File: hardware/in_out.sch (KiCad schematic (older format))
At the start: 41 parts

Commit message: changed heirarchy labels, changed diode and inductor to standard library symbols
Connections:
- net pd0_i2c_scl renamed i2c_scl
- net pd1_i2c_sda renamed i2c_sda
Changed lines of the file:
@@
-EESchema Schematic File Version 2  date Thu 31 Oct 2013 01:30:22 PM EDT
+EESchema Schematic File Version 2  date Mon 04 Nov 2013 07:38:03 AM EST
 LIBS:power
 LIBS:device
@@
 Sheet 4 5
 Title ""
-Date "31 oct 2013"
+Date "4 nov 2013"
 Rev ""
 Comp ""
@@
 $EndComp
 Text HLabel 1450 5700 0    60   Input ~ 0
-pd1_i2c_sda
+i2c_sda
 Text HLabel 1450 5550 0    60   Input ~ 0
-pd0_i2c_scl
+i2c_scl
 $Comp
 L +3.3V #PWR?

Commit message: cleaned up most of the error check problems
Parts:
- gave numbers to parts that had none: 41
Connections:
- no-connect marks 0 -> 4

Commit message: added RCT and accellerometer, added new sheet
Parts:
- removed C15, C16: 3000 uF, symbol C
- removed D4, D5, D6, D7: BAT54J, 1206, symbol BAT54J
- removed R18, R22: 1K, symbol R
- removed R21, R23: 220, symbol R
- removed R24, R36: 10K, symbol R
- removed R25, R38: 33.2K, symbol R
- removed T1, T2: BUZ11, symbol BUZ11
- removed U7, U8: SN74LVC1G14, symbol SN74LVC1G14
- added BT?: BATTERY, symbol BATTERY
- added C? (x3): 0.1 uF, symbol C
- added C?: 4.7 uF, symbol C
- added R? (x3): 2K, symbol R
- added U?: DS1307, symbol DS1307
- added U?: MMA8451Q, symbol MMA8451Q
- added X?: 32.768KHz, symbol CRYSTAL
- R23: renamed from R19; value 1K -> 2K
- R24: renamed from R20; value 1K -> 2K
- renumbered C14 to C19, Q1 to Q4, Q2 to Q5, Q3 to Q6, Q4 to Q7, R16 to R20, R17 to R21, R26 to R30, R27 to R31, R28 to R32, R29 to R33, R30 to R34, R31 to R35, R32 to R36, R33 to R37, R34 to R38, R35 to R39, R37 to R41, R39 to R43
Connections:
- net +3.3V: now also R?.1, R?.1, U?.1 (Vddio), U?.14 (Vdd)
- net +5V: now also C?.1, C?.1, R?.1, U?.8 (Vcc)
- net GND: now also BT?.2 (-), C?.2, C?.2, C?.2, C?.2, U?.10 (gnd), U?.12 (gnd), U?.4 (gnd), U?.5 (gnd)
- net i2c_scl: now also U?.4 (scl), U?.6 (scl)
- net i2c_sda: now also U?.5 (sda), U?.6 (sda)
- new net: U?.1 (X1), X?.1
- new net: U?.2 (X2), X?.2
- new net: BT?.1 (+), U?.3 (Vbat)
- new net: C?.1, U?.2 (byp)
- new net accel_int_0: R?.2, U?.11 (int1)
- new net accel_int_1: R?.2, U?.9 (int2)
- new net square_wave: R?.2, U?.7 (sqw_out)
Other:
- note added: "12.5 pF\n"
- note added: "Li 48 >48 mA"
- moved on the sheet: C19, P2, Q4, Q5, Q6, Q7, R20, R21, R23, R24, R30, R31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

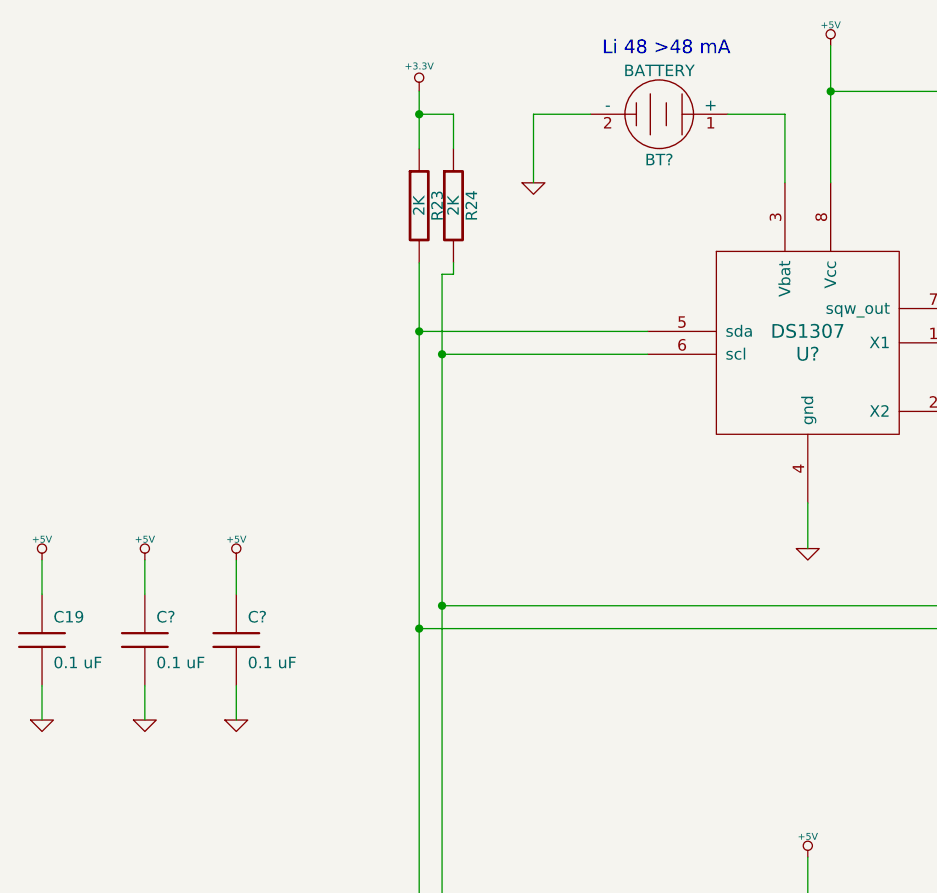
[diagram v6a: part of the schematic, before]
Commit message: fixed heirarchy connections for modified sheets
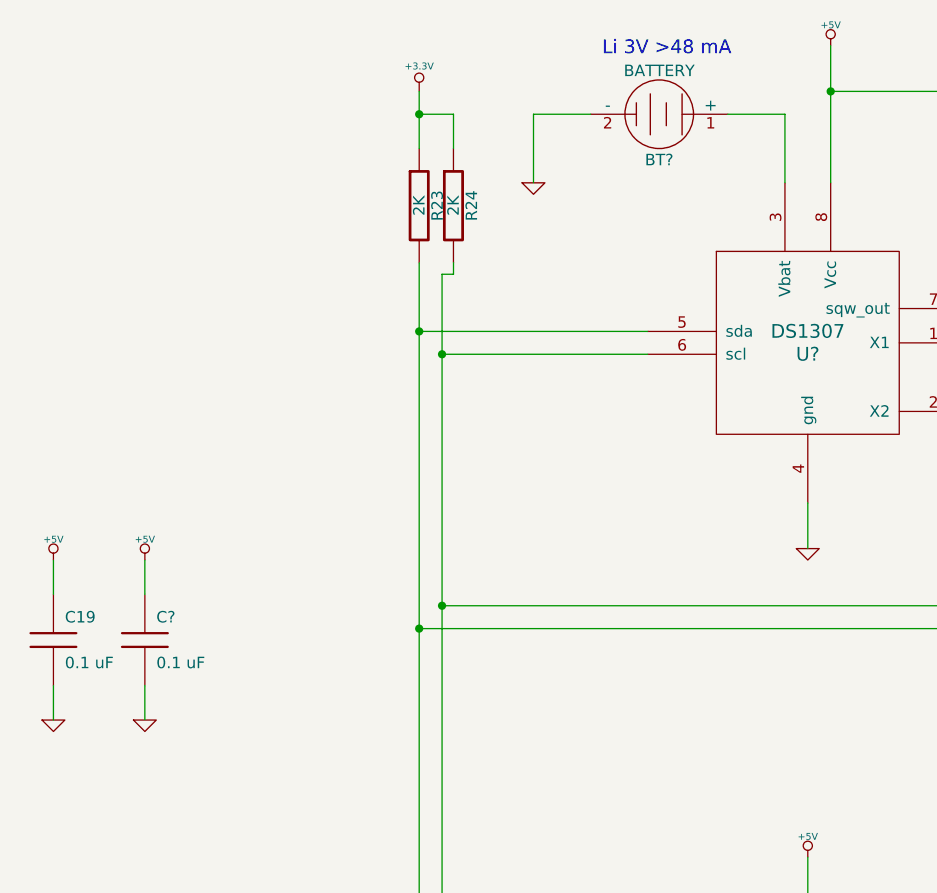
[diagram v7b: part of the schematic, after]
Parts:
- removed C?: 0.1 uF, symbol C
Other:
- note added: "Li 3V >48 mA"
- note removed: "Li 48 >48 mA"
- moved on the sheet: C19
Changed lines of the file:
@@
-EESchema Schematic File Version 2  date Tue 12 Nov 2013 10:09:33 PM EST
+EESchema Schematic File Version 2  date Wed 13 Nov 2013 08:13:39 AM EST
 LIBS:power
 LIBS:device
@@
 	6650 2200 7850 2200
 Wire Wire Line
-	1700 3600 1700 3750
-Wire Wire Line
-	1700 3200 1700 3050
-Wire Wire Line
 	1300 3200 1300 3050
 Wire Wire Line
@@
 	4300 1400 4300 800
 Wire Wire Line
-	850  3600 850  3750
+	900  3600 900  3750
 Wire Wire Line
 	1200 6250 1200 6500
@@
 	1350 6300 1350 6250
 Wire Wire Line
-	850  3200 850  3050
+	900  3200 900  3050
 Wire Wire Line
 	4200 3000 4200 2800
@@
 $EndComp
 $Comp
-L GND #PWR?
-U 1 1 5282D633
-P 1700 3750
-F 0 "#PWR?" H 1700 3750 30  0001 C CNN
-F 1 "GND" H 1700 3680 30  0001 C CNN
-	1    1700 3750
-	1    0    0    -1
-$EndComp
-$Comp
-L +5V #PWR?
-U 1 1 5282D632
-P 1700 3050
-F 0 "#PWR?" H 1700 3140 20  0001 C CNN
-F 1 "+5V" H 1700 3140 30  0000 C CNN
-	1    1700 3050
-	1    0    0    -1
-$EndComp
-$Comp
-L C C?
-U 1 1 5282D631
-P 1700 3400
-F 0 "C?" H 1750 3500 50  0000 L CNN
-F 1 "0.1 uF" H 1750 3300 50  0000 L CNN
-	1    1700 3400
-	1    0    0    -1
-$EndComp
-$Comp
 L C C?
 U 1 1 5282D617
@@
 $EndComp
 Text Notes 3300 850  0    60   ~ 0
-Li 48 >48 mA
+Li 3V >48 mA
 Text Notes 5800 2750 0    60   ~ 0
 12.5 pF\n
@@
 L GND #PWR022
 U 1 1 526E4C5E
-P 850 3750
-F 0 "#PWR022" H 850 3750 30  0001 C CNN
-F 1 "GND" H 850 3680 30  0001 C CNN
-	1    850  3750
+P 900 3750
+F 0 "#PWR022" H 900 3750 30  0001 C CNN
+F 1 "GND" H 900 3680 30  0001 C CNN
+	1    900  3750
 	1    0    0    -1
 $EndComp
@@
 L +5V #PWR023
 U 1 1 526E4C55
-P 850 3050
-F 0 "#PWR023" H 850 3140 20  0001 C CNN
-F 1 "+5V" H 850 3140 30  0000 C CNN
-	1    850  3050
+P 900 3050
+F 0 "#PWR023" H 900 3140 20  0001 C CNN
+F 1 "+5V" H 900 3140 30  0000 C CNN
+	1    900  3050
 	1    0    0    -1
 $EndComp
@@
 L C C19
 U 1 1 526E4C4C
-P 850 3400
-F 0 "C19" H 900 3500 50  0000 L CNN
-F 1 "0.1 uF" H 900 3300 50  0000 L CNN
-	1    850  3400
-	1    0    0    -1
-$EndComp
+P 900 3400
+F 0 "C19" H 950 3500 50  0000 L CNN
+F 1 "0.1 uF" H 950 3300 50  0000 L CNN
+	1    900  3400
+	1    0    0    -1
+$EndComp

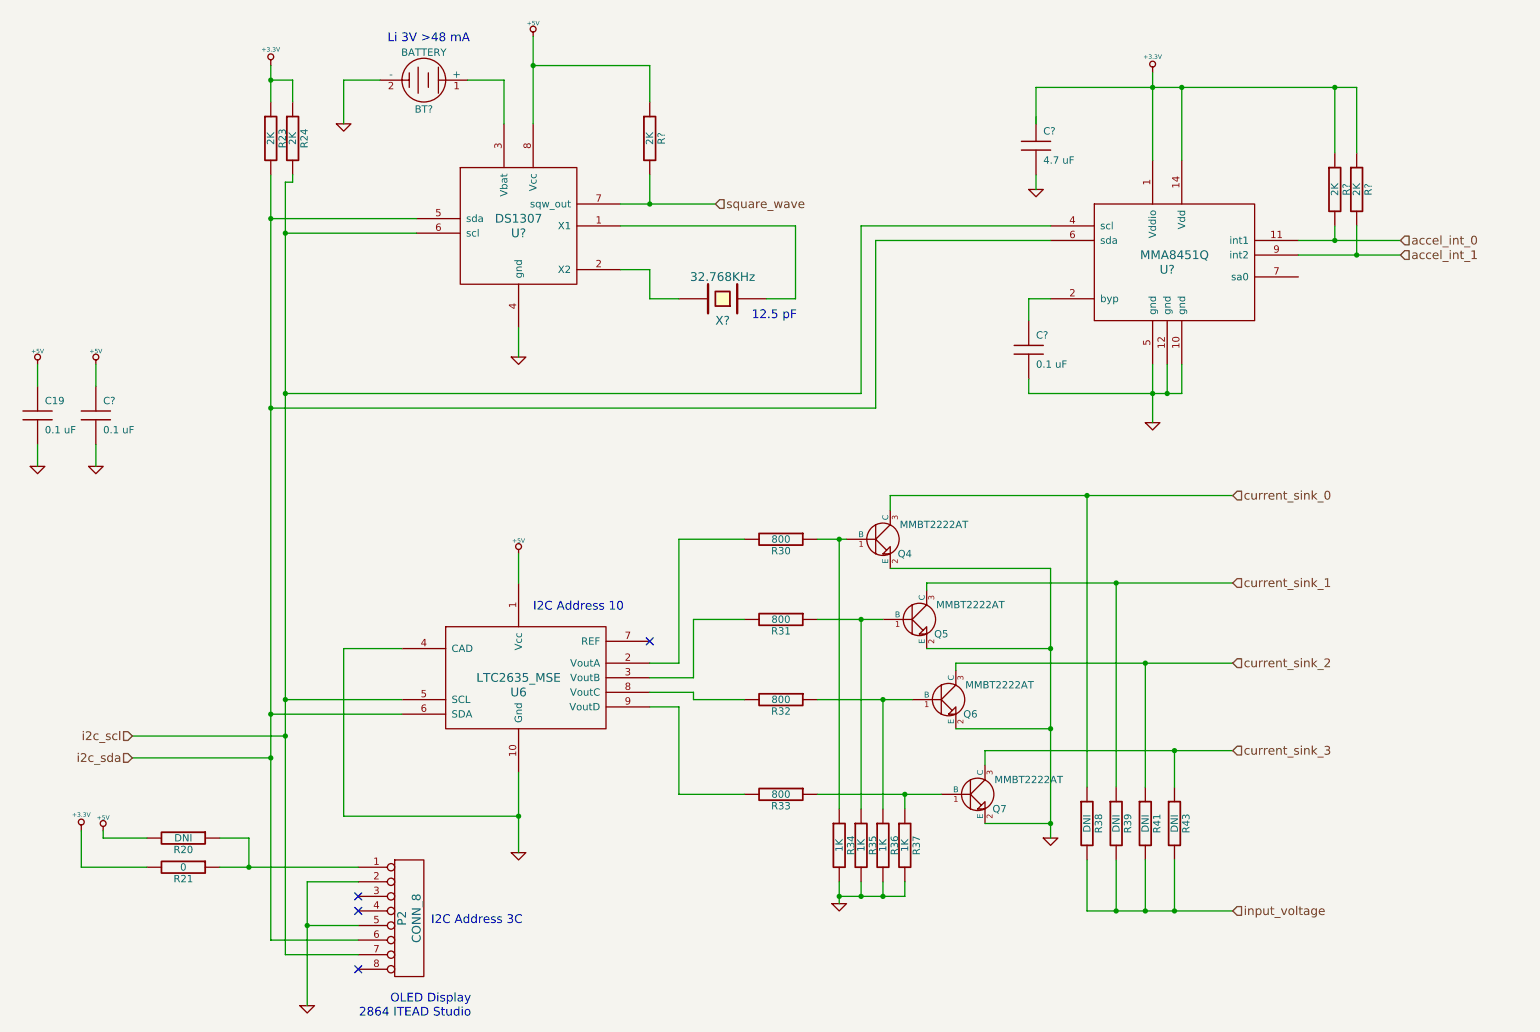
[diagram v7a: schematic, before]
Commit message: removed jtag header and changed the rtc
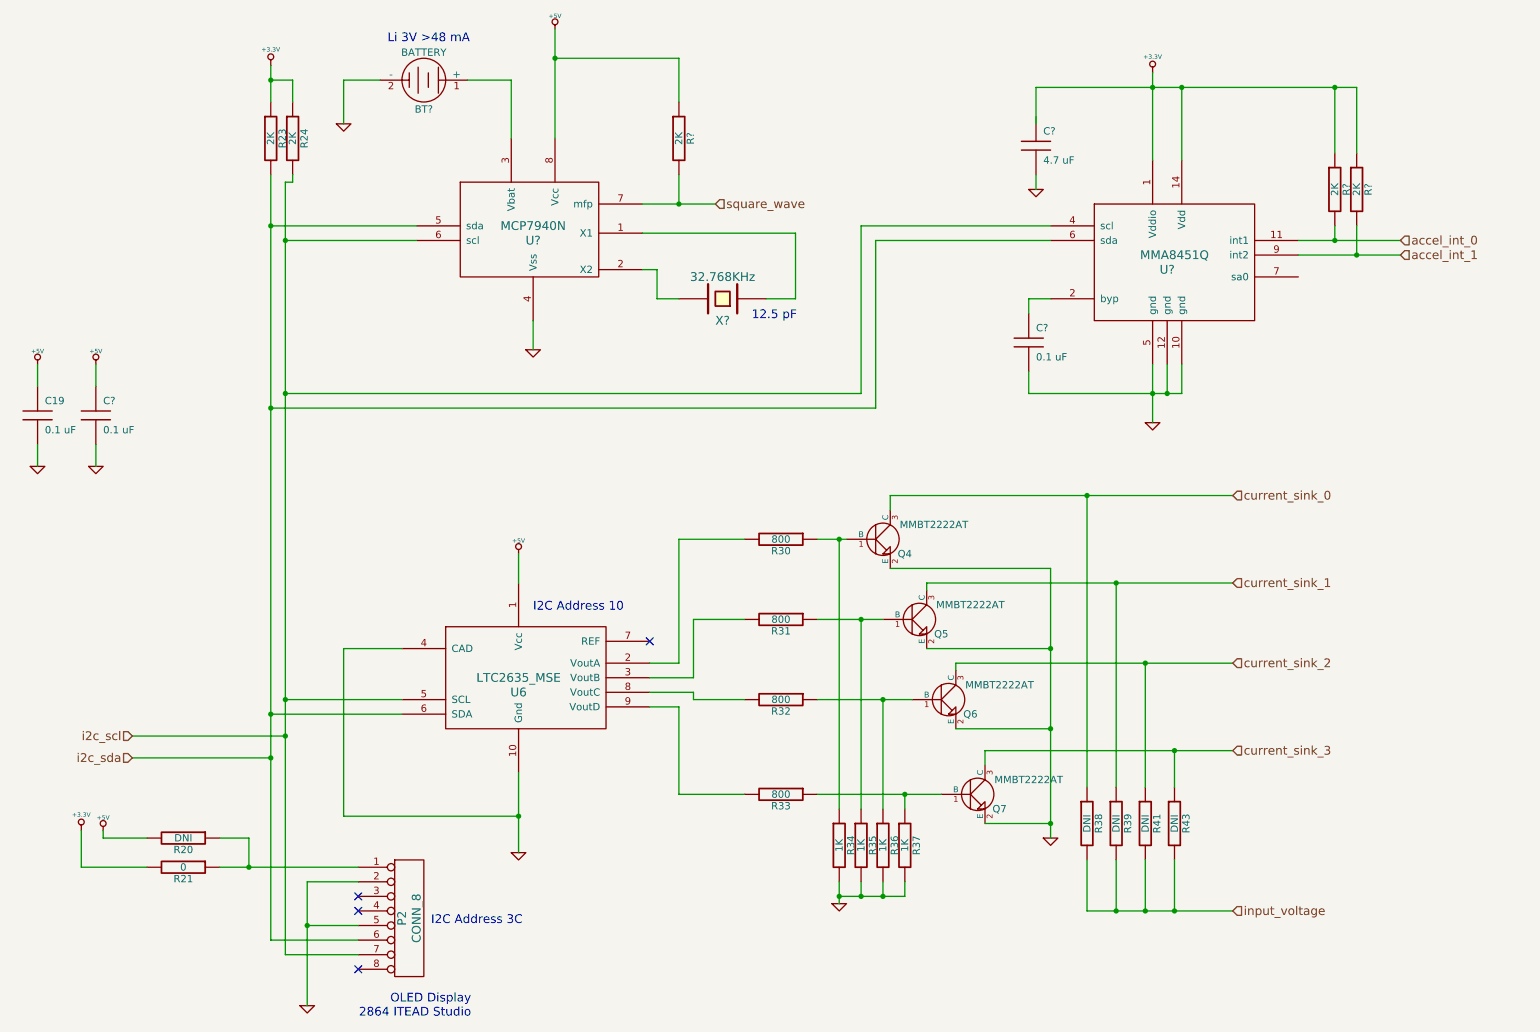
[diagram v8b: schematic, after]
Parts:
- removed U?: DS1307, symbol DS1307
- added U?: MCP7940N, symbol MCP7940N
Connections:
- net +5V: now also U?.8 (Vcc)
- net GND: now also U?.4 (Vss)
- net i2c_scl: now also U?.6 (scl)
- net i2c_sda: now also U?.5 (sda)
- net square_wave: now also U?.7 (mfp)
- net at X?.1: now also U?.1 (X1)
- net at X?.2: now also U?.2 (X2)
- net at BT?.1 (+): now also U?.3 (Vbat)
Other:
- moved on the sheet: C?, R?
